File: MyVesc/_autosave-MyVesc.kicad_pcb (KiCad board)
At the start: 4 copper layers, 100 x 70 mm, 112 parts, among them J1 CAN, J10 GATE_PH_A, J11 CURR_SENS_PH_A, J12 CURR_SENS_PH_B, J13 CURR_SENS_PH_C, J14 Pull_up, J2 Conn_01x08, J4 Conn_01x03, J5 UNUSED MCU PINS, J6 TEMP_SENS, J7 V_IN, J8 GATE_PH_C, J9 GATE_PH_B, P4 HALL/Encoder, P5 SWD, U1 TJA1051T/3/1J, U10 LM5161, U11 MCP16311/2, U12 MCP16311/2, U13 INA240, U14 INA240, U15 INA240, U2 BMI160, U3 STM32F405RGT6, U4 UCC2721x, U5 UCC2721x, U6 UCC2721x, Y1 8M

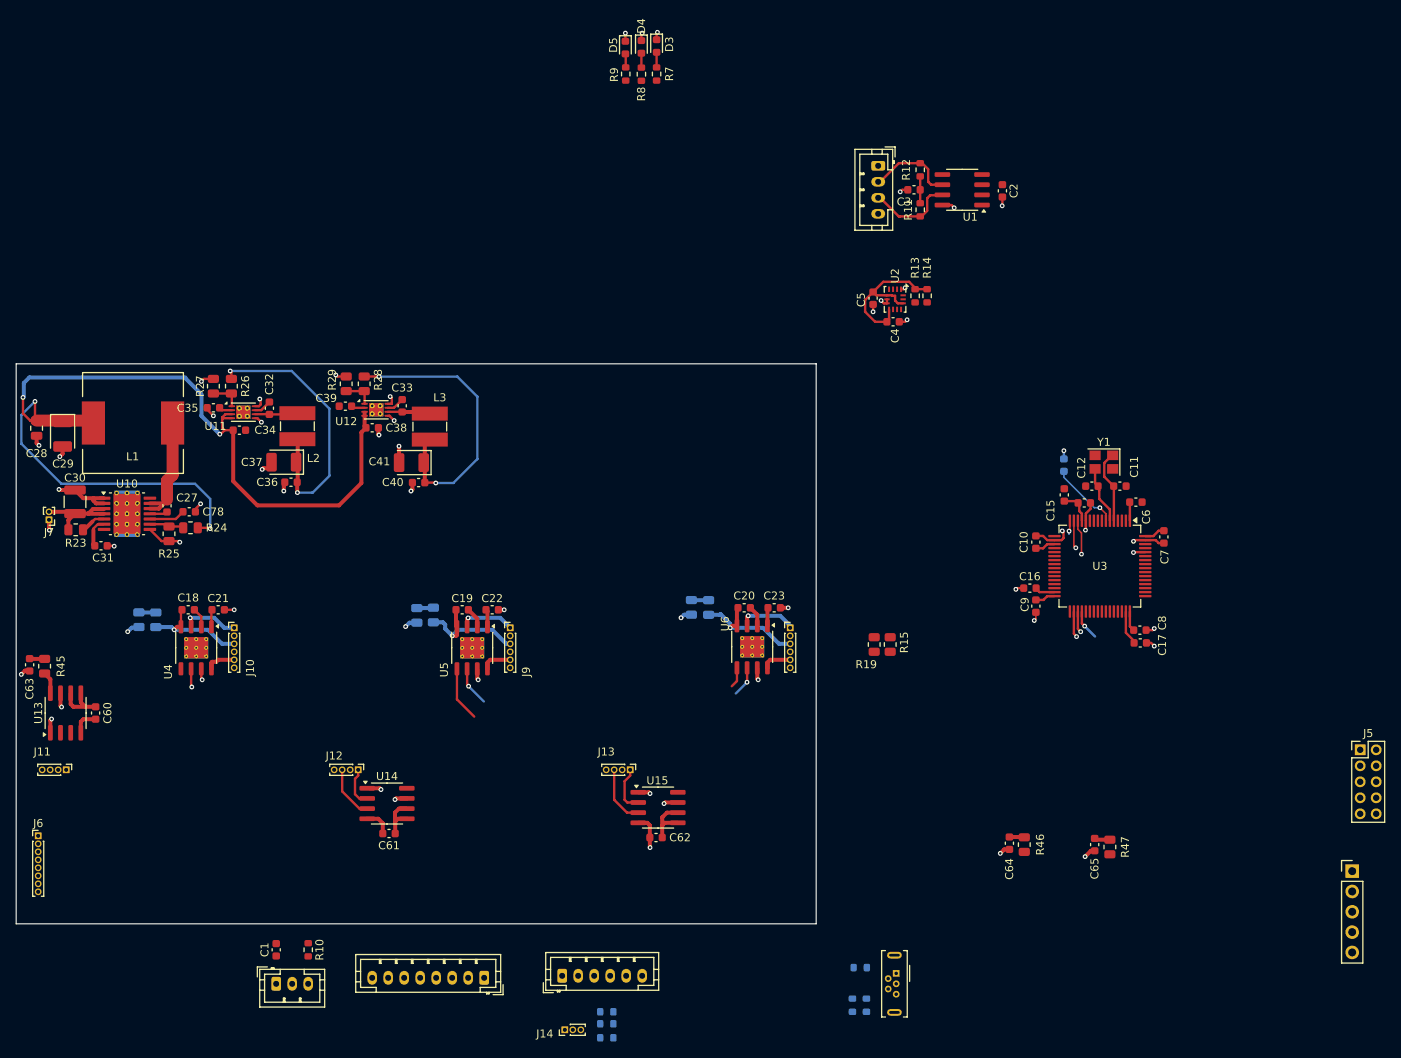
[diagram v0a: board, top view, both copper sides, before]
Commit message: updated board for new mosfets
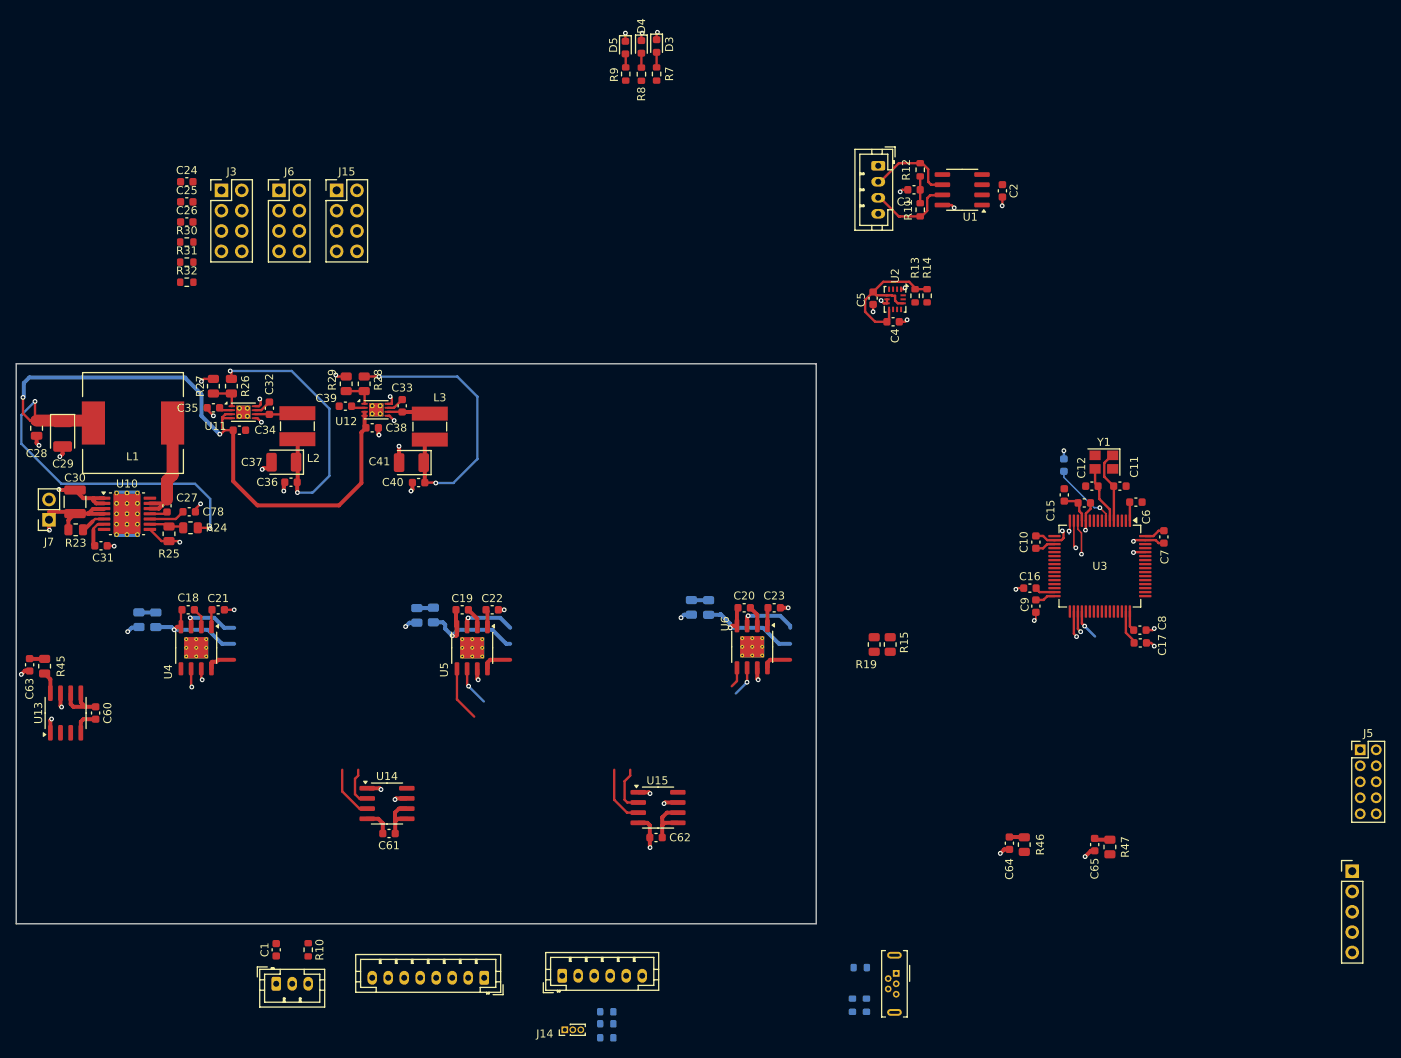
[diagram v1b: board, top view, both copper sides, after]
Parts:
- removed J10: GATE_PH_A, Connector_PinHeader_1.00mm:PinHeader_1x06_P1.00mm_Vertical
- removed J11: CURR_SENS_PH_A, Connector_PinHeader_1.00mm:PinHeader_1x04_P1.00mm_Vertical
- removed J12: CURR_SENS_PH_B, Connector_PinHeader_1.00mm:PinHeader_1x04_P1.00mm_Vertical
- removed J13: CURR_SENS_PH_C, Connector_PinHeader_1.00mm:PinHeader_1x04_P1.00mm_Vertical
- removed J8: GATE_PH_C, Connector_PinHeader_1.00mm:PinHeader_1x06_P1.00mm_Vertical
- removed J9: GATE_PH_B, Connector_PinHeader_1.00mm:PinHeader_1x06_P1.00mm_Vertical
- added C24: 2.2u, Capacitor_SMD:C_0603_1608Metric, F.Cu at (51.1, 164.8)
- added C25: 2.2u, Capacitor_SMD:C_0603_1608Metric, F.Cu at (51.1, 167.3)
- added C26: 2.2u, Capacitor_SMD:C_0603_1608Metric, F.Cu at (51.1, 169.8)
- added J15: PH_C_CONNECTOR, Connector_PinHeader_2.54mm:PinHeader_2x04_P2.54mm_Vertical, F.Cu at (69.8, 165.8)
- added J3: PH_A_CONNECTOR, Connector_PinHeader_2.54mm:PinHeader_2x04_P2.54mm_Vertical, F.Cu at (55.4, 165.8)
- added R30: 10k, Resistor_SMD:R_0603_1608Metric, F.Cu at (51.1, 172.3)
- added R31: 10k, Resistor_SMD:R_0603_1608Metric, F.Cu at (51.1, 174.8)
- added R32: 10k, Resistor_SMD:R_0603_1608Metric, F.Cu at (51.1, 177.3)
- J6: value TEMP_SENS -> PH_B_CONNECTOR; footprint Connector_PinHeader_1.00mm:PinHeader_1x08_P1.00mm_Vertical -> Connector_PinHeader_2.54mm:PinHeader_2x04_P2.54mm_Vertical
- J7: footprint Connector_PinHeader_1.00mm:PinHeader_1x02_P1.00mm_Vertical -> Connector_PinSocket_2.54mm:PinSocket_1x02_P2.54mm_Vertical
- moved J6 86.1 mm to (62.6, 165.8)
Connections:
- J6 pad 1: VCC -> /Power MOSFETS/PH_B_IN+
- J6 pad 2: GND -> /Power MOSFETS/PH_B_IN-
- J6 pad 3: /MCU/ADC_TEMP3 -> GND
- J6 pad 4: GND -> /Power MOSFETS/TEMP2
- J6 pad 5: /MCU/ADC_TEMP2 -> /Mosfet driver/LO2
- J6 pad 6: GND -> VCC
- J6 pad 7: /MCU/ADC_TEMP -> /Mosfet driver/HS2
- J6 pad 8: GND -> /Mosfet driver/HO2
- U13 pad 2: Net-(J11-Pin_1) -> /Power MOSFETS/PH_A_IN+
- U13 pad 3: Net-(J11-Pin_3) -> /Power MOSFETS/PH_A_IN-
- U14 pad 2: Net-(J12-Pin_1) -> /Power MOSFETS/PH_B_IN+
- U14 pad 3: Net-(J12-Pin_3) -> /Power MOSFETS/PH_B_IN-
- U15 pad 2: Net-(J13-Pin_1) -> /Power MOSFETS/PH_C_IN+
- U15 pad 3: Net-(J13-Pin_3) -> /Power MOSFETS/PH_C_IN-
- U3 pad 17: /MCU/ADC_TEMP -> /Power MOSFETS/TEMP
- U3 pad 26: /MCU/ADC_TEMP2 -> /Power MOSFETS/TEMP2
- U3 pad 27: /MCU/ADC_TEMP3 -> /Power MOSFETS/TEMP3
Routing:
- net Net-(J13-Pin_3): track 7.42 -> 0.00 mm
- net /Power MOSFETS/PH_C_IN-: track 0.00 -> 7.42 mm
- net Net-(J12-Pin_3): track 6.72 -> 0.00 mm
- net /Power MOSFETS/PH_B_IN-: track 0.00 -> 6.72 mm
- net Net-(J13-Pin_1): track 5.88 -> 0.00 mm
- net /Power MOSFETS/PH_C_IN+: track 0.00 -> 5.88 mm
- net Net-(J12-Pin_1): track 4.96 -> 0.00 mm
- net /Power MOSFETS/PH_B_IN+: track 0.00 -> 4.96 mm
